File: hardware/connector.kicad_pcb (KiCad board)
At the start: 4 copper layers, 20 x 22 mm, 2 parts, among them J1 AXK5F20347YG, J2 AXK5F20347YG

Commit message: :sparkles: assembly all the part!
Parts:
- moved J1 23.1 mm to (140.2, 98.8)
- moved J2 23.1 mm to (153.2, 98.8)

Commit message: :bug: improve hardware design
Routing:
- net P,+3.3: track 16.3 -> 8.21 mm

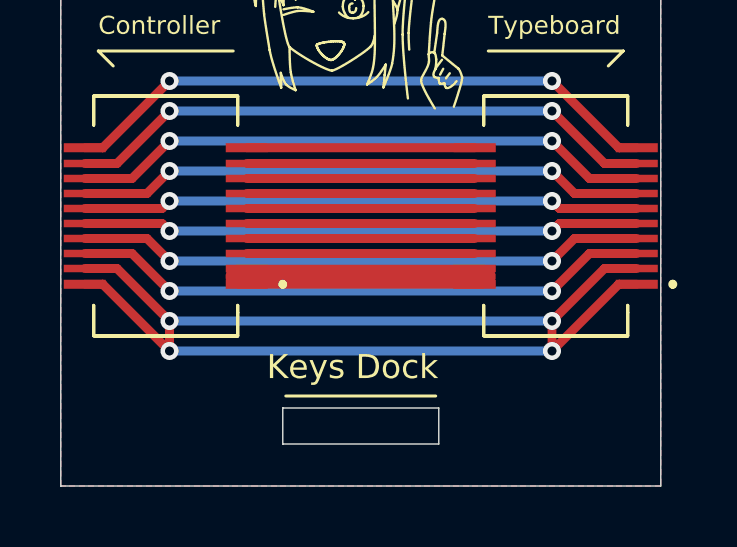
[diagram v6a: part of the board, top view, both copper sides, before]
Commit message: :zap: improve led power supply
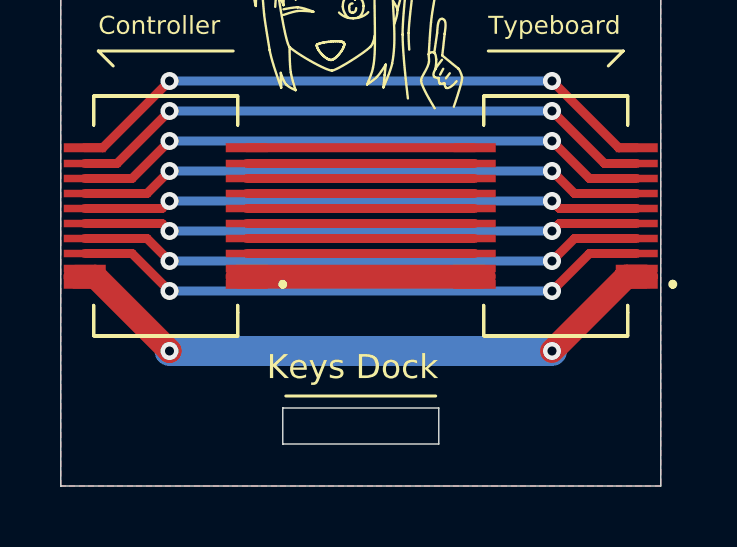
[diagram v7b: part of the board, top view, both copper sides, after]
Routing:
- net P,+5: track 42.1 -> 21.1 mm, vias 4 -> 2
